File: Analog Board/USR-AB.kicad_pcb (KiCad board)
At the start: 2 copper layers, 129.5 x 61.1 mm, 6 parts, among them J2 S5B-XH-A_LF__SN_, J3 S5B-XH-A_LF__SN_, U2 CD74HC4067SM96, U3 SC0918

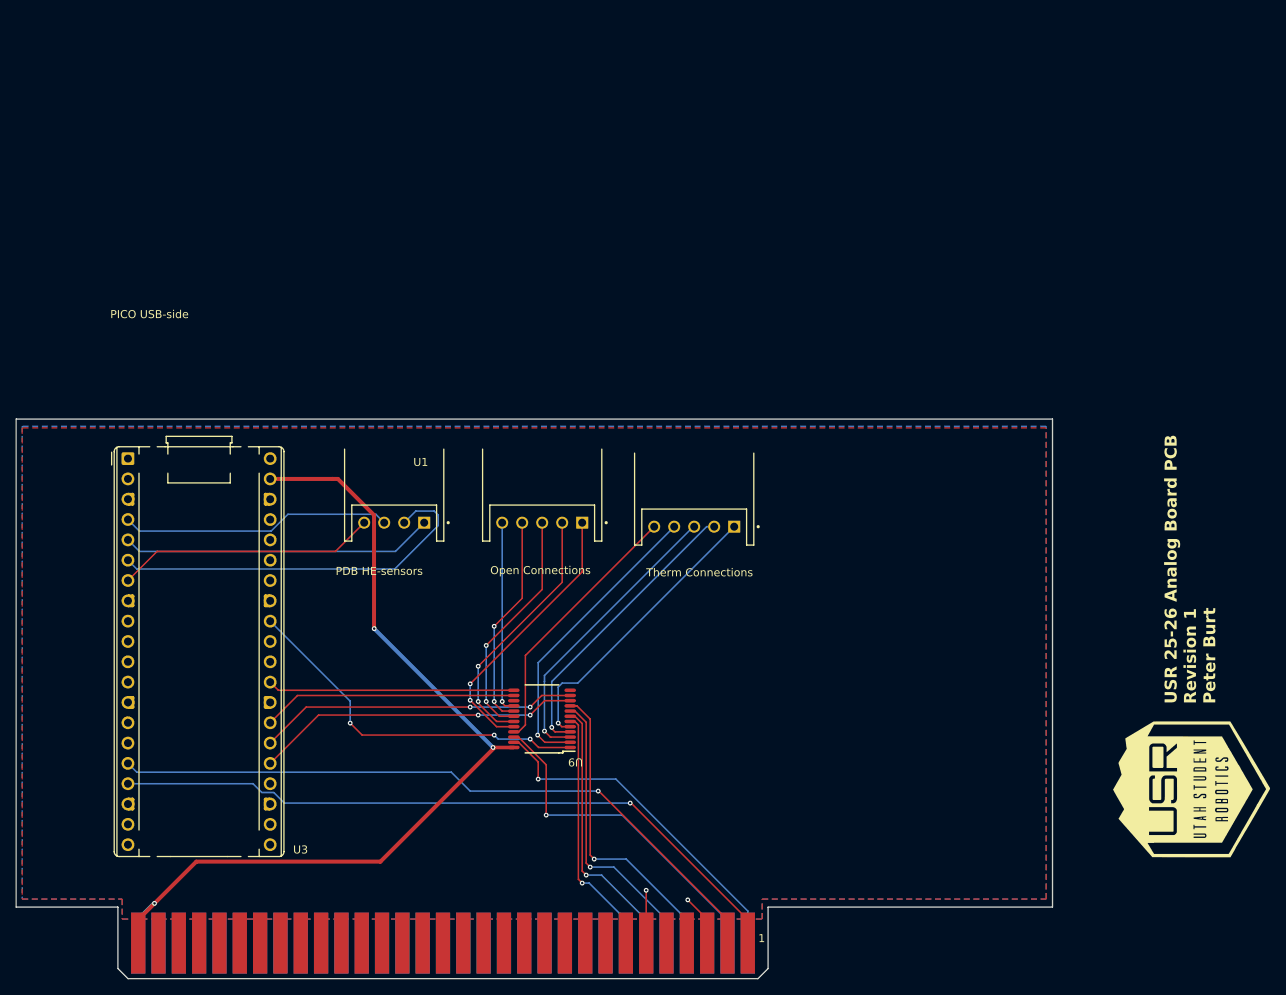
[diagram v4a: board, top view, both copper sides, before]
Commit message: Added board dimension info onto the PCB, updated silkscreen
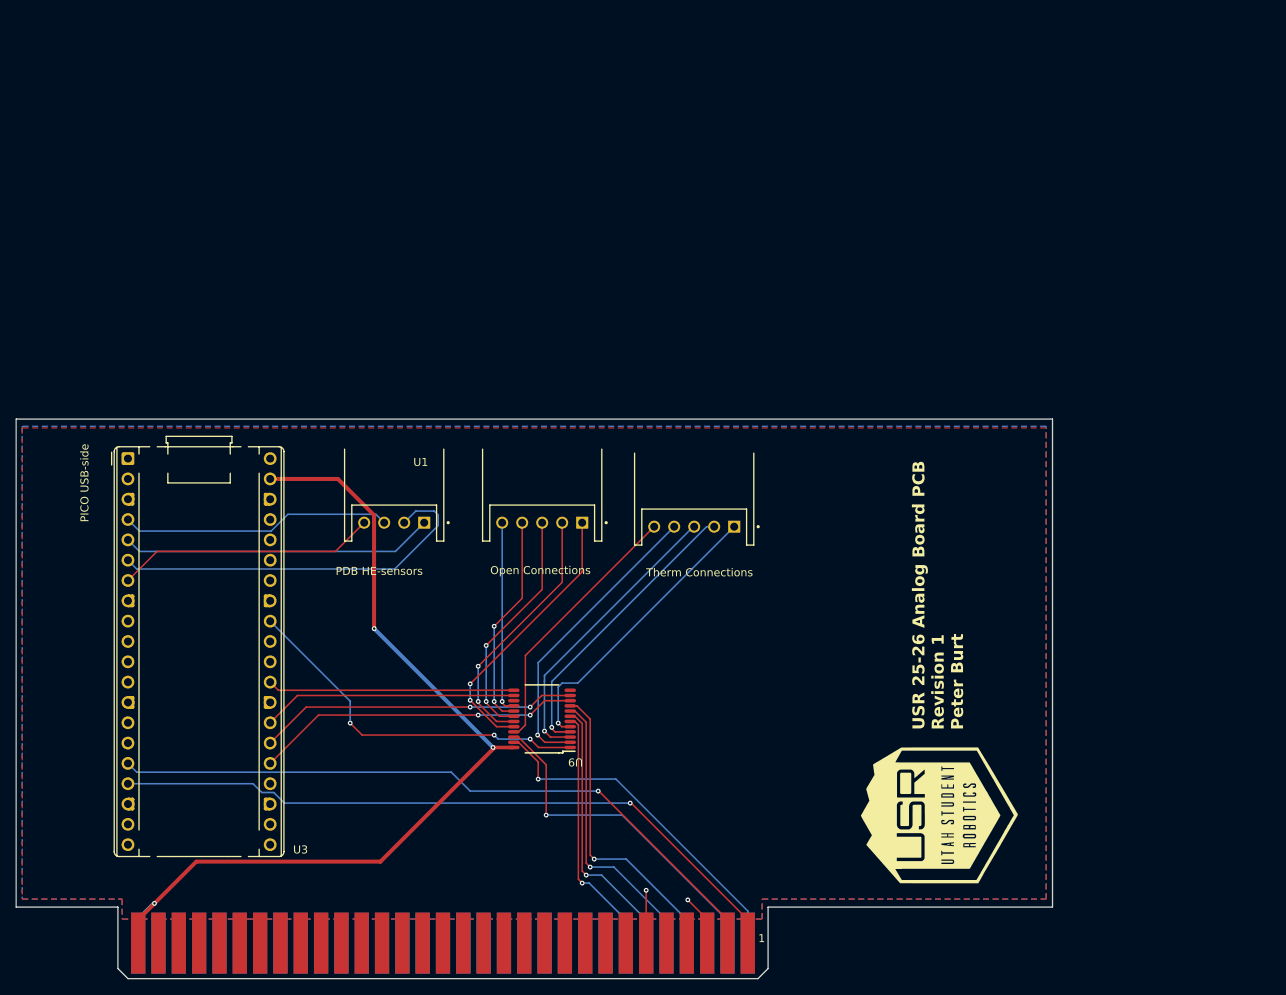
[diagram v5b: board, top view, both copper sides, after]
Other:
- board text removed: "shorten height of the board"

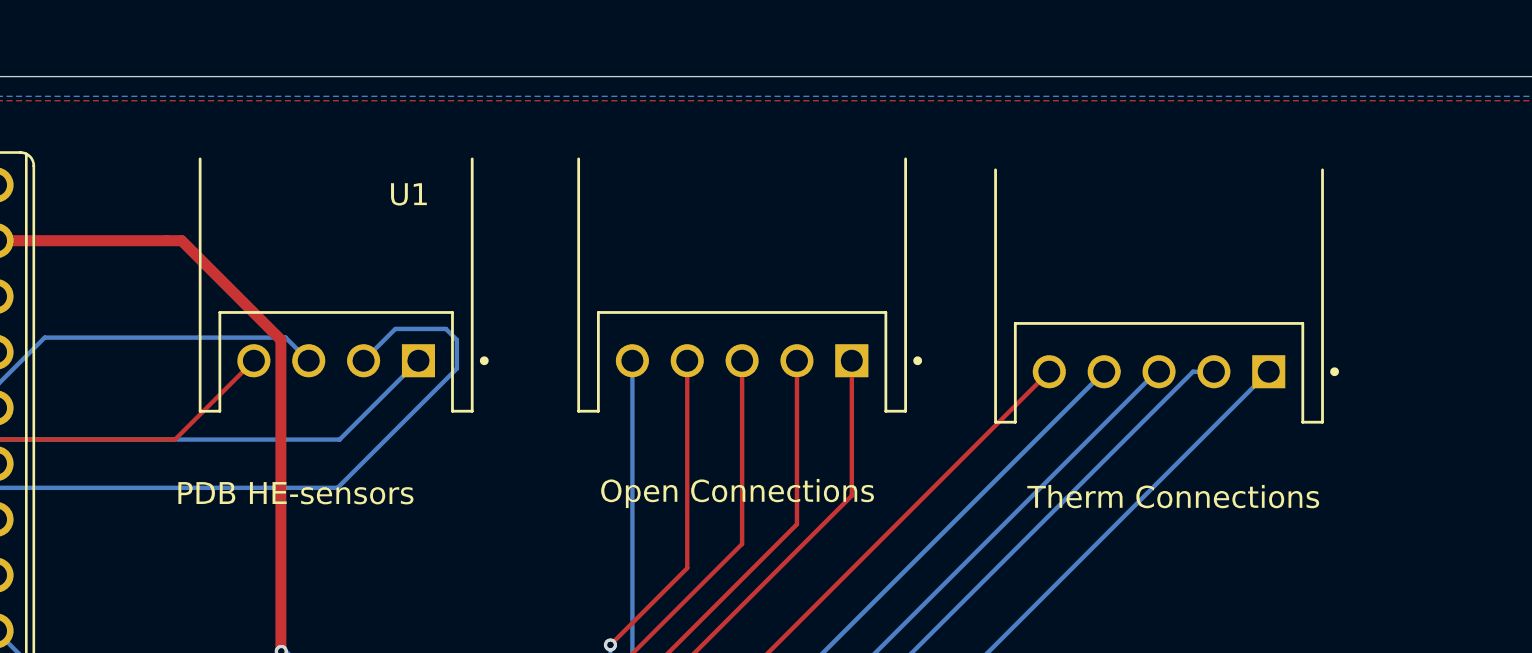
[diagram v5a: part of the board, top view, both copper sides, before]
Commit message: added silkscreen labels to ports on analog board
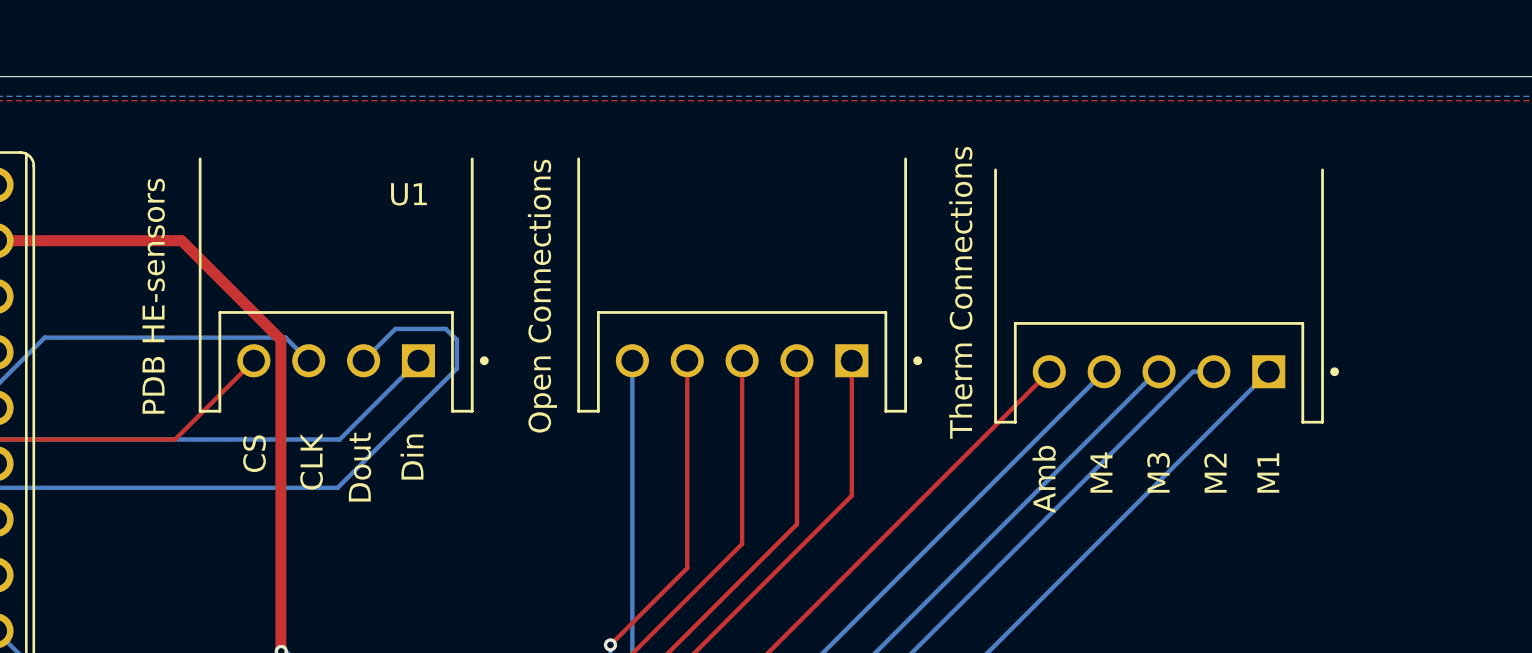
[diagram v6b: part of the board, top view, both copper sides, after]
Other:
- board text added: "Amb"
- board text added: "CLK"
- board text added: "CS"
- board text added: "Din"
- board text added: "Dout"
- board text added: "M1"
- board text added: "M2"
- board text added: "M3"
- board text added: "M4"
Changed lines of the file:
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@@
 		(layer "Edge.Cuts")
 	)
+	(gr_text "PICO USB-side"
+		(at 47.4 97.4 90)
+		(layer "F.SilkS")
+		(effects
+			(font
+				(size 1 1)
+				(thickness 0.1)
+			)
+			(justify left bottom)
+		)
+	)
 	(gr_text "PDB HE-sensors"
-		(at 78.175 104.1 0)
+		(at 77.8 100 90)
+		(layer "F.SilkS")
+		(effects
+			(font
+				(size 1 1)
+				(thickness 0.1)
+			)
+			(justify left bottom)
+		)
+	)
+	(gr_text "CS"
+		(at 82.4 102.6 90)
+		(layer "F.SilkS")
+		(effects
+			(font
+				(size 1 1)
+				(thickness 0.1)
+			)
+			(justify left bottom)
+		)
+	)
+	(gr_text "CLK"
+		(at 85 103.4 90)
+		(layer "F.SilkS")
+		(effects
+			(font
+				(size 1 1)
+				(thickness 0.1)
+			)
+			(justify left bottom)
+		)
+	)
+	(gr_text "Dout"
+		(at 87.2 104 90)
+		(layer "F.SilkS")
+		(effects
+			(font
+				(size 1 1)
+				(thickness 0.1)
+			)
+			(justify left bottom)
+		)
+	)
+	(gr_text "Din"
+		(at 89.6 103 90)
 		(layer "F.SilkS")
 		(effects
@@
 	)
 	(gr_text "Open Connections"
-		(at 97.5 104 0)
+		(at 95.4 100.8 90)
 		(layer "F.SilkS")
 		(effects
@@
 	)
 	(gr_text "Therm Connections"
-		(at 117 104.275 0)
+		(at 114.6 101 90)
 		(layer "F.SilkS")
 		(effects
@@
 		)
 	)
-	(gr_text "PICO USB-side"
-		(at 47.4 97.4 90)
+	(gr_text "Amb"
+		(at 118.4 104.4 90)
 		(layer "F.SilkS")
 		(effects
+			(font
+				(size 1 1)
+				(thickness 0.1)
+			)
+			(justify left bottom)
+		)
+	)
+	(gr_text "M4"
+		(at 121 103.6 90)
+		(layer "F.SilkS")
+		(effects
+			(font
+				(size 1 1)
+				(thickness 0.1)
+			)
+			(justify left bottom)
+		)
+	)
+	(gr_text "M3"
+		(at 123.6 103.6 90)
+		(layer "F.SilkS")
+		(effects
+			(font
+				(size 1 1)
+				(thickness 0.1)
+			)
+			(justify left bottom)
+		)
+	)
+	(gr_text "M2"
+		(at 126.2 103.6 90)
+		(layer "F.SilkS")
+		(effects
+			(font
+				(size 1 1)
+				(thickness 0.1)
+			)
+			(justify left bottom)
+		)
+	)
+	(gr_text "M1"
+		(at 128.6 103.6 90)
+		(layer "F.SilkS")
+		(effects

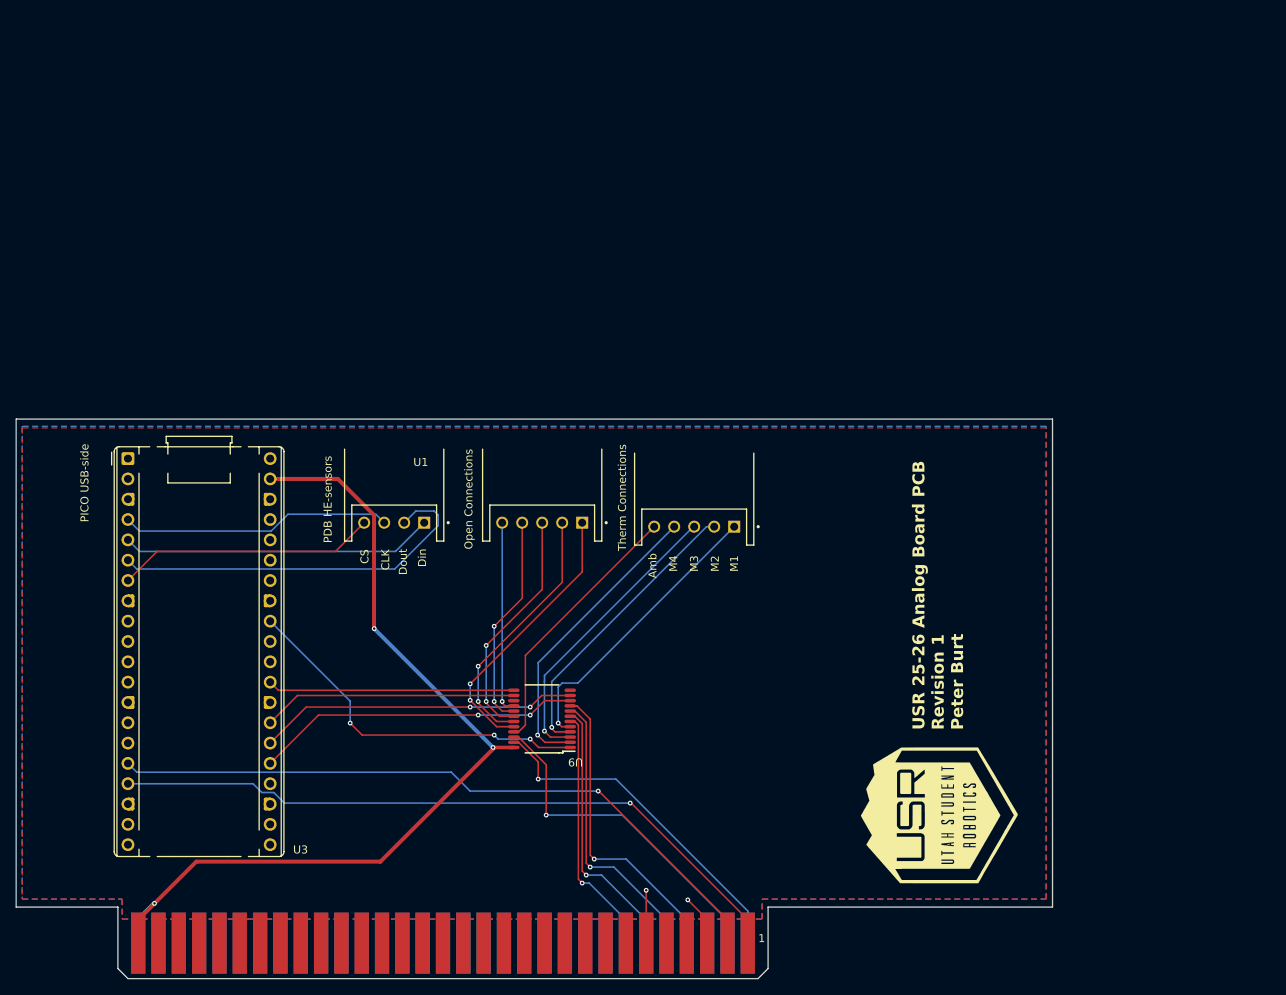
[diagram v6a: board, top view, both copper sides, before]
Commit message: Finalized designs for MCU card, Analog board, and MDCB
Added additional vias to all in order to minimize ground loops and stitch together front and back ground planes.
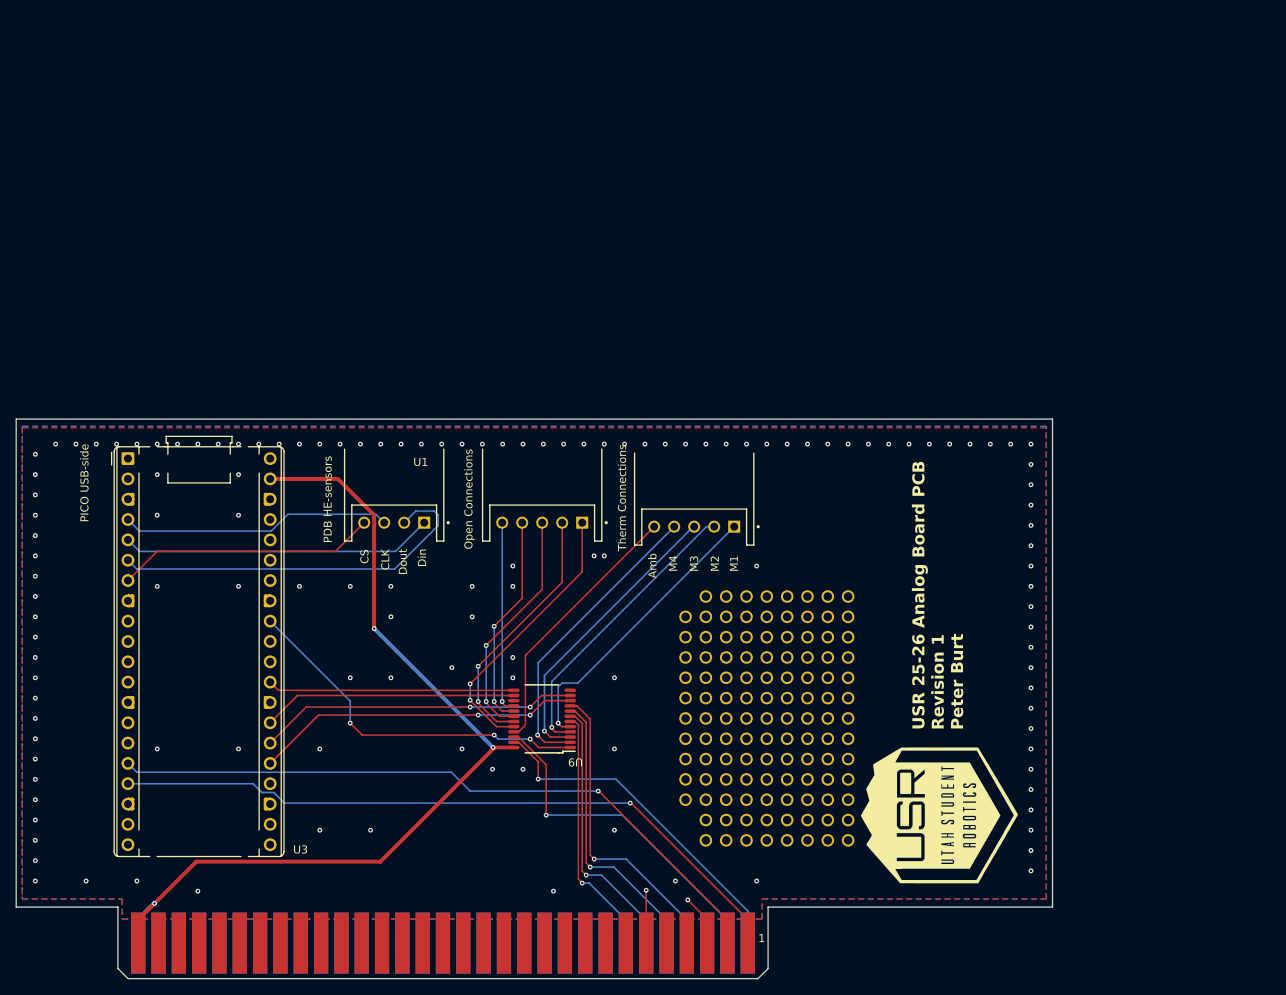
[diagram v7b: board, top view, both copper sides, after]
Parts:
- added ?: , , F.Cu at (134.6, 134.6)
- added ?: , , F.Cu at (134.6, 109.2)
- added ?: , , F.Cu at (139.7, 137.2)
- added ?: , , F.Cu at (127.0, 114.3)
- added ?: , , F.Cu at (127.0, 137.2)
- added ?: , , F.Cu at (121.9, 119.4)
- added ?: , , F.Cu at (129.5, 132.1)
- added ?: , , F.Cu at (139.7, 109.2)
- added ?: , , F.Cu at (129.5, 119.4)
- added ?: , , F.Cu at (127.0, 106.7)
- added ?: , , F.Cu at (137.2, 119.4)
- added ?: , , F.Cu at (137.2, 124.5)
- added ?: , , F.Cu at (137.2, 137.2)
- added ?: , , F.Cu at (142.2, 116.8)
- added ?: , , F.Cu at (134.6, 121.9)
- added ?: , , F.Cu at (134.6, 114.3)
- added ?: , , F.Cu at (132.1, 114.3)
- added ?: , , F.Cu at (124.5, 132.1)
- added ?: , , F.Cu at (134.6, 111.8)
- added ?: , , F.Cu at (127.0, 109.2)
- added ?: , , F.Cu at (137.2, 121.9)
- added ?: , , F.Cu at (121.9, 111.8)
- added ?: , , F.Cu at (139.7, 106.7)
- added ?: , , F.Cu at (124.5, 106.7)
- added ?: , , F.Cu at (142.2, 127.0)
- added ?: , , F.Cu at (142.2, 134.6)
- added ?: , , F.Cu at (121.9, 116.8)
- added ?: , , F.Cu at (127.0, 129.5)
- added ?: , , F.Cu at (121.9, 114.3)
- added ?: , , F.Cu at (132.1, 106.7)
- added ?: , , F.Cu at (134.6, 137.2)
- added ?: , , F.Cu at (142.2, 124.5)
- added ?: , , F.Cu at (121.9, 109.2)
- added ?: , , F.Cu at (129.5, 134.6)
- added ?: , , F.Cu at (137.2, 111.8)
- added ?: , , F.Cu at (124.5, 124.5)
- added ?: , , F.Cu at (142.2, 132.1)
- added ?: , , F.Cu at (132.1, 119.4)
- added ?: , , F.Cu at (142.2, 137.2)
- added ?: , , F.Cu at (129.5, 114.3)
- added ?: , , F.Cu at (137.2, 127.0)
- added ?: , , F.Cu at (134.6, 132.1)
- added ?: , , F.Cu at (127.0, 119.4)
- added ?: , , F.Cu at (139.7, 132.1)
- added ?: , , F.Cu at (124.5, 127.0)
- added ?: , , F.Cu at (142.2, 114.3)
- added ?: , , F.Cu at (142.2, 106.7)
- added ?: , , F.Cu at (132.1, 129.5)
- added ?: , , F.Cu at (132.1, 124.5)
- added ?: , , F.Cu at (139.7, 114.3)
- added ?: , , F.Cu at (139.7, 116.8)
- added ?: , , F.Cu at (121.9, 124.5)
- added ?: , , F.Cu at (127.0, 127.0)
- added ?: , , F.Cu at (129.5, 129.5)
- added ?: , , F.Cu at (142.2, 119.4)
- added ?: , , F.Cu at (127.0, 132.1)
- added ?: , , F.Cu at (129.5, 127.0)
- added ?: , , F.Cu at (137.2, 114.3)
- added ?: , , F.Cu at (124.5, 109.2)
- added ?: , , F.Cu at (124.5, 134.6)
- added ?: , , F.Cu at (139.7, 124.5)
- added ?: , , F.Cu at (142.2, 121.9)
- added ?: , , F.Cu at (139.7, 127.0)
- added ?: , , F.Cu at (124.5, 119.4)
- added ?: , , F.Cu at (139.7, 111.8)
- added ?: , , F.Cu at (142.2, 109.2)
- added ?: , , F.Cu at (124.5, 129.5)
- added ?: , , F.Cu at (121.9, 127.0)
- added ?: , , F.Cu at (129.5, 109.2)
- added ?: , , F.Cu at (127.0, 134.6)
- added ?: , , F.Cu at (121.9, 121.9)
- added ?: , , F.Cu at (134.6, 116.8)
- added ?: , , F.Cu at (124.5, 114.3)
- added ?: , , F.Cu at (132.1, 109.2)
- added ?: , , F.Cu at (124.5, 111.8)
- added ?: , , F.Cu at (134.6, 129.5)
- added ?: , , F.Cu at (129.5, 121.9)
- added ?: , , F.Cu at (132.1, 116.8)
- added ?: , , F.Cu at (129.5, 111.8)
- added ?: , , F.Cu at (139.7, 121.9)
- added ?: , , F.Cu at (132.1, 121.9)
- added ?: , , F.Cu at (139.7, 134.6)
- added ?: , , F.Cu at (142.2, 129.5)
- added ?: , , F.Cu at (132.1, 132.1)
- added ?: , , F.Cu at (129.5, 124.5)
- added ?: , , F.Cu at (124.5, 121.9)
- added ?: , , F.Cu at (132.1, 127.0)
- added ?: , , F.Cu at (139.7, 119.4)
- added ?: , , F.Cu at (129.5, 137.2)
- added ?: , , F.Cu at (137.2, 132.1)
- added ?: , , F.Cu at (127.0, 121.9)
- added ?: , , F.Cu at (124.5, 137.2)
- added ?: , , F.Cu at (142.2, 111.8)
- added ?: , , F.Cu at (137.2, 109.2)
- added ?: , , F.Cu at (134.6, 127.0)
- added ?: , , F.Cu at (129.5, 106.7)
- added ?: , , F.Cu at (129.5, 116.8)
- added ?: , , F.Cu at (121.9, 132.1)
- added ?: , , F.Cu at (137.2, 129.5)
- added ?: , , F.Cu at (127.0, 116.8)
- added ?: , , F.Cu at (134.6, 124.5)
- added ?: , , F.Cu at (137.2, 106.7)
- added ?: , , F.Cu at (121.9, 129.5)
- added ?: , , F.Cu at (137.2, 134.6)
- added ?: , , F.Cu at (132.1, 111.8)
- added ?: , , F.Cu at (127.0, 111.8)
- added ?: , , F.Cu at (127.0, 124.5)
- added ?: , , F.Cu at (139.7, 129.5)
- added ?: , , F.Cu at (137.2, 116.8)
- added ?: , , F.Cu at (132.1, 137.2)
- added ?: , , F.Cu at (132.1, 134.6)
- added ?: , , F.Cu at (134.6, 106.7)
- added ?: , , F.Cu at (124.5, 116.8)
- added ?: , , F.Cu at (134.6, 119.4)
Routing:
- net GND: vias 2 -> 133
